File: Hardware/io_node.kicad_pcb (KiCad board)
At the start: 2 copper layers, 60 x 90 mm, 133 parts, among them J1 Conn_01x09, J2 Conn_01x09, J3 Conn_01x09, J4 Conn_01x05, J5 USB_B_Micro, J6 Conn_01x05, J7 Conn_01x05, J8 Conn_01x02, J9 Conn_01x04, Q1 2N7002, Q2 2N7002, Q3 2N7002, Q4 2N7002, Q5 2N7002, Q6 2N7002, Q7 2N7002, Q8 2N7002, U1 STM32F103RBT6, U10 EL357N-G, U11 EL357N-G, U12 EL357N-G, U13 EL357N-G, U14 EL357N-G, U15 USBLC6-2SC6, U2 AMS1117-5.0, U3 AMS1117-3.3, U4 SP3485EN, U5 TLV274CPWR, U6 TLV274CPWR, U7 EL357N-G, U8 EL357N-G, U9 EL357N-G, Y1 8 MHz

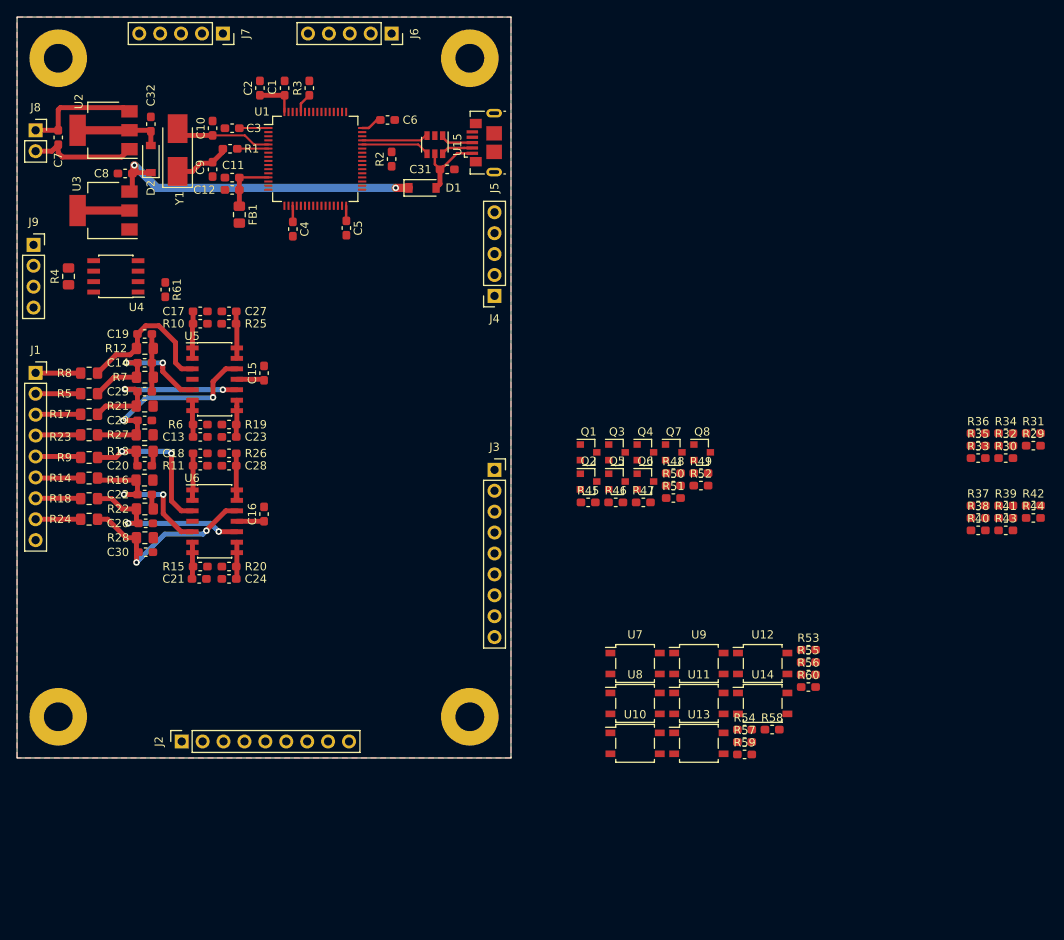
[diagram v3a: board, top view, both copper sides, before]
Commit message: Layout DIN DOT
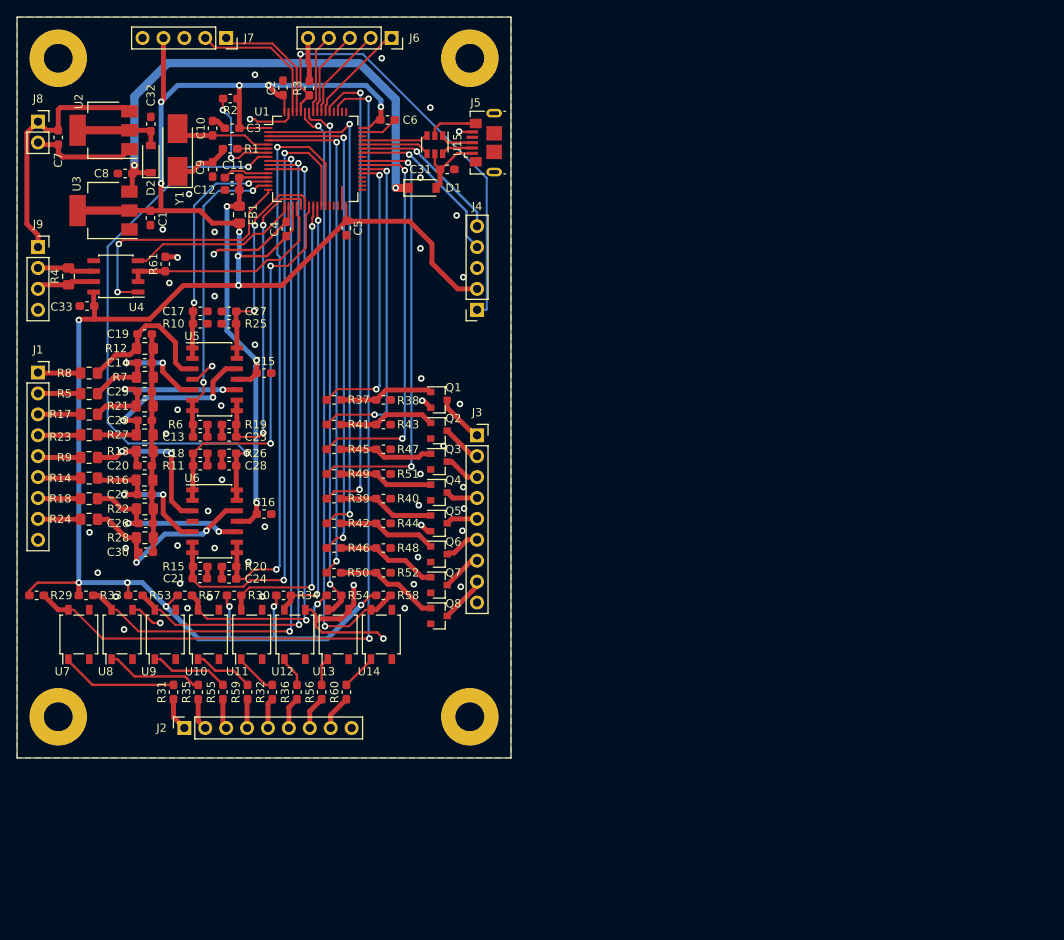
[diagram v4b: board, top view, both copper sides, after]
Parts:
- added C33: 100NF, Capacitor_SMD:C_0603_1608Metric_Pad1.05x0.95mm_HandSolder, F.Cu at (53.5, 50.1)
- moved R29 122.4 mm to (47.4, 85.2)
- moved R33 109.7 mm to (53.4, 85.2)
- moved R31 109.1 mm to (64.0, 97.0), turned to 90 degrees
- moved R35 99.4 mm to (67.0, 97.0), turned to 90 degrees
- moved R30 95.2 mm to (71.4, 85.2)
- moved R32 94.0 mm to (76.0, 97.0), turned to 90 degrees
- moved R34 89.9 mm to (77.4, 85.2)
- moved R36 88.5 mm to (79.0, 97.0), turned to 90 degrees
- moved R42 85.0 mm to (83.5, 76.5)
- moved R41 82.4 mm to (83.5, 64.5)
- moved R53 82.0 mm to (59.4, 85.2)
- moved R39 81.6 mm to (83.5, 73.5)
- moved R37 79.3 mm to (83.5, 61.5)
- moved R44 79.0 mm to (89.5, 76.5)
- moved R43 76.7 mm to (89.5, 64.5)
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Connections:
- Q1 pad 3: /TIM3_CH1 -> /Output/DOT_0
- Q2 pad 3: /OUT_4 -> /Output/DOT_1
- Q3 pad 3: /TIM3_CH2 -> /Output/DOT_2
- Q4 pad 3: /OUT_5 -> /Output/DOT_3
- Q5 pad 3: /TIM3_CH3 -> /Output/DOT_4
- Q6 pad 3: /OUT_6 -> /Output/DOT_5
- Q7 pad 3: /TIM3_CH4 -> /Output/DOT_6
- Q8 pad 3: /OUT_7 -> /Output/DOT_7
- R29 pad 2: /Input/DIN_0 -> /IN_0
- R30 pad 2: /Input/DIN_4 -> /IN_4
- R31 pad 1: /IN_0 -> /Input/DIN_0
- R32 pad 1: /IN_4 -> /Input/DIN_4
- R33 pad 2: /Input/DIN_1 -> /IN_1
- R34 pad 2: /Input/DIN_5 -> /IN_5
- R35 pad 1: /IN_1 -> /Input/DIN_1
- R36 pad 1: /IN_5 -> /Input/DIN_5
- R37 pad 1: /Output/DOT_0 -> /TIM3_CH1
- R39 pad 1: /Output/DOT_4 -> /OUT_4
- R39 pad 2: Net-(Q2-Pad1) -> Net-(Q5-Pad1)
- R40 pad 1: Net-(Q2-Pad1) -> Net-(Q5-Pad1)
- R41 pad 1: /Output/DOT_1 -> /TIM3_CH2
- R41 pad 2: Net-(Q3-Pad1) -> Net-(Q2-Pad1)
- R42 pad 1: /Output/DOT_5 -> /OUT_5
- R42 pad 2: Net-(Q4-Pad1) -> Net-(Q6-Pad1)
- R43 pad 1: Net-(Q3-Pad1) -> Net-(Q2-Pad1)
- R44 pad 1: Net-(Q4-Pad1) -> Net-(Q6-Pad1)
- R45 pad 1: /Output/DOT_2 -> /TIM3_CH3
- R45 pad 2: Net-(Q5-Pad1) -> Net-(Q3-Pad1)
- R46 pad 1: /Output/DOT_6 -> /OUT_6
- R46 pad 2: Net-(Q6-Pad1) -> Net-(Q7-Pad1)
- R47 pad 1: Net-(Q5-Pad1) -> Net-(Q3-Pad1)
- R48 pad 1: Net-(Q6-Pad1) -> Net-(Q7-Pad1)
- R49 pad 1: /Output/DOT_3 -> /TIM3_CH4
- R49 pad 2: Net-(Q7-Pad1) -> Net-(Q4-Pad1)
- R50 pad 1: /Output/DOT_7 -> /OUT_7
- R51 pad 1: Net-(Q7-Pad1) -> Net-(Q4-Pad1)
- R53 pad 2: /Input/DIN_2 -> /IN_2
- R54 pad 2: /Input/DIN_6 -> /IN_6
- R55 pad 1: /IN_2 -> /Input/DIN_2
- R56 pad 1: /IN_6 -> /Input/DIN_6
- R57 pad 2: /Input/DIN_3 -> /IN_3
- R58 pad 2: /Input/DIN_7 -> /IN_7
- R59 pad 1: /IN_3 -> /Input/DIN_3
- R60 pad 1: /IN_7 -> /Input/DIN_7
- U1 pad 28: /SPI1_CS -> Net-(U1-Pad28)
- U1 pad 54: Net-(U1-Pad54) -> /SPI1_CS
- U10 pad 1: Net-(R36-Pad2) -> Net-(R59-Pad2)
- U10 pad 4: /Input/DIN_5 -> /IN_3
- U11 pad 1: Net-(R55-Pad2) -> Net-(R32-Pad2)
- U11 pad 4: /Input/DIN_2 -> /IN_4
- U12 pad 1: Net-(R56-Pad2) -> Net-(R36-Pad2)
- U12 pad 4: /Input/DIN_6 -> /IN_5
- U13 pad 1: Net-(R59-Pad2) -> Net-(R56-Pad2)
- U13 pad 4: /Input/DIN_3 -> /IN_6
- U14 pad 4: /Input/DIN_7 -> /IN_7
- U4 pad 8: +3.3VA -> +3V3
- U7 pad 4: /Input/DIN_0 -> /IN_0
- U8 pad 1: Net-(R32-Pad2) -> Net-(R35-Pad2)
- U8 pad 4: /Input/DIN_4 -> /IN_1
- U9 pad 1: Net-(R35-Pad2) -> Net-(R55-Pad2)
- U9 pad 4: /Input/DIN_1 -> /IN_2
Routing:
- net +3V3: track 21.3 -> 271.9 mm, vias 0 -> 16
- net /IN_0: track 0.00 -> 112.2 mm, vias 0 -> 2
- net GND: track 24.0 -> 125.2 mm, vias 0 -> 53
- net /IN_1: track 0.00 -> 86.1 mm, vias 0 -> 2
- net /IN_2: track 0.00 -> 80.5 mm, vias 0 -> 2
- net /IN_3: track 0.00 -> 75.0 mm, vias 0 -> 2
- net /ADC_IN8: track 4.48 -> 78.3 mm, vias 0 -> 2
- net /IN_7: track 0.00 -> 73.4 mm, vias 0 -> 2
- net /ADC_IN9: track 4.49 -> 73.2 mm, vias 0 -> 2
- net /ADC_IN10: track 6.49 -> 71.6 mm, vias 0 -> 2
- net /IN_6: track 0.00 -> 64.0 mm, vias 0 -> 2
- net /OUT_7: track 0.00 -> 61.2 mm, vias 0 -> 2
- net /OUT_5: track 0.00 -> 60.9 mm, vias 0 -> 2
- net /OUT_6: track 0.00 -> 60.4 mm, vias 0 -> 2
- net /OUT_4: track 0.00 -> 57.8 mm, vias 0 -> 2
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
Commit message: Add SWD
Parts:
- added J10: Conn_01x04, Connector_PinSocket_2.54mm:PinSocket_1x04_P2.54mm_Vertical, F.Cu at (93.3, 17.5)
- moved J6 7.40 mm to (83.1, 17.5)
- moved J7 2.54 mm to (67.9, 17.5)
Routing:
- net /NRST: track 12.4 -> 45.7 mm, vias 2 -> 3
- net /ADC_IN10: track 71.6 -> 53.3 mm
- net /SWDIO: track 0.00 -> 14.1 mm
- net /SWCLK: track 0.00 -> 13.9 mm
- net GND: track 125.2 -> 134.0 mm, vias 53 -> 135
- net /SPI1_MOSI: track 9.77 -> 13.1 mm
- net /SPI1_CS: track 12.6 -> 9.24 mm
- net /USART2_TX: track 31.1 -> 28.1 mm
- net /BOOT0: track 53.9 -> 51.6 mm
- net /I2C1_SCL: track 15.4 -> 17.3 mm
- net /I2C1_SDA: track 17.4 -> 19.2 mm
- net /SPI1_SCK: track 11.5 -> 9.76 mm
- net +5V: track 61.7 -> 60.4 mm
- net +3V3: track 271.9 -> 272.7 mm
- net /ADC_IN9: track 73.2 -> 72.5 mm
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
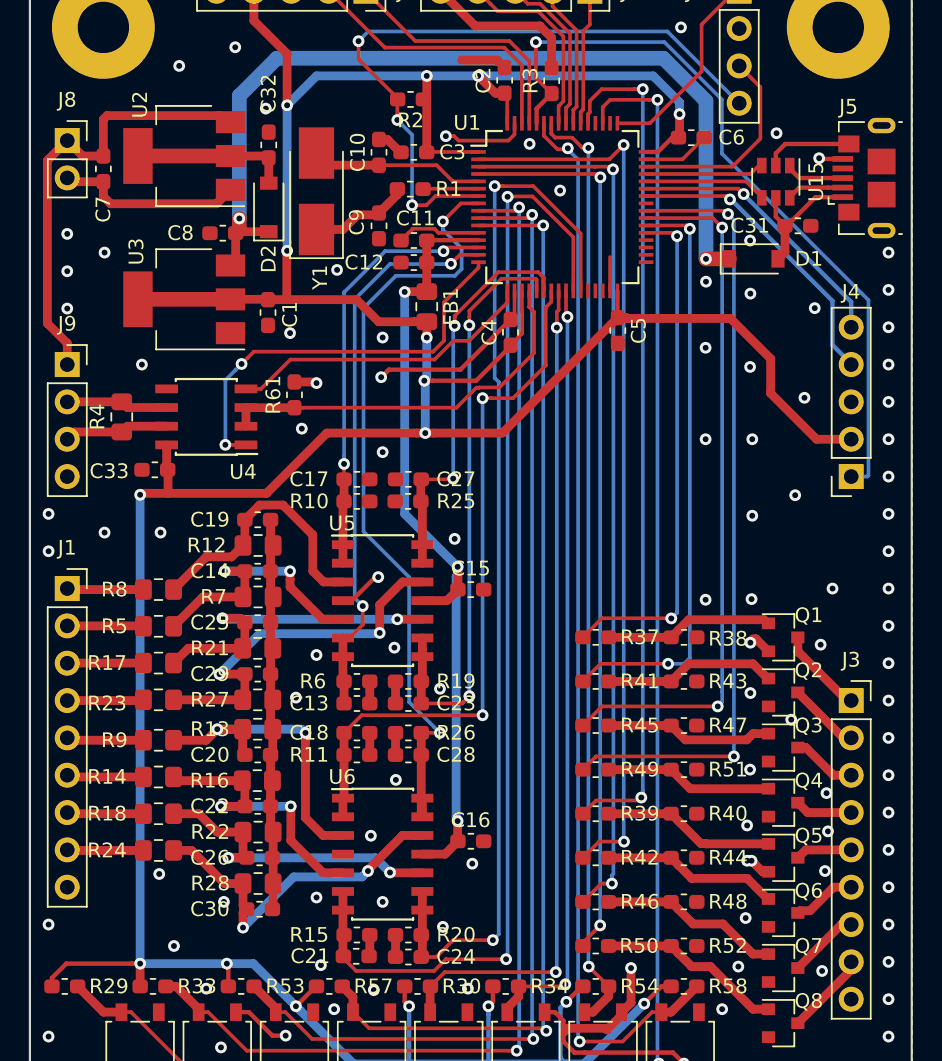
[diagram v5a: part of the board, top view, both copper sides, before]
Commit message: Update USB footprint
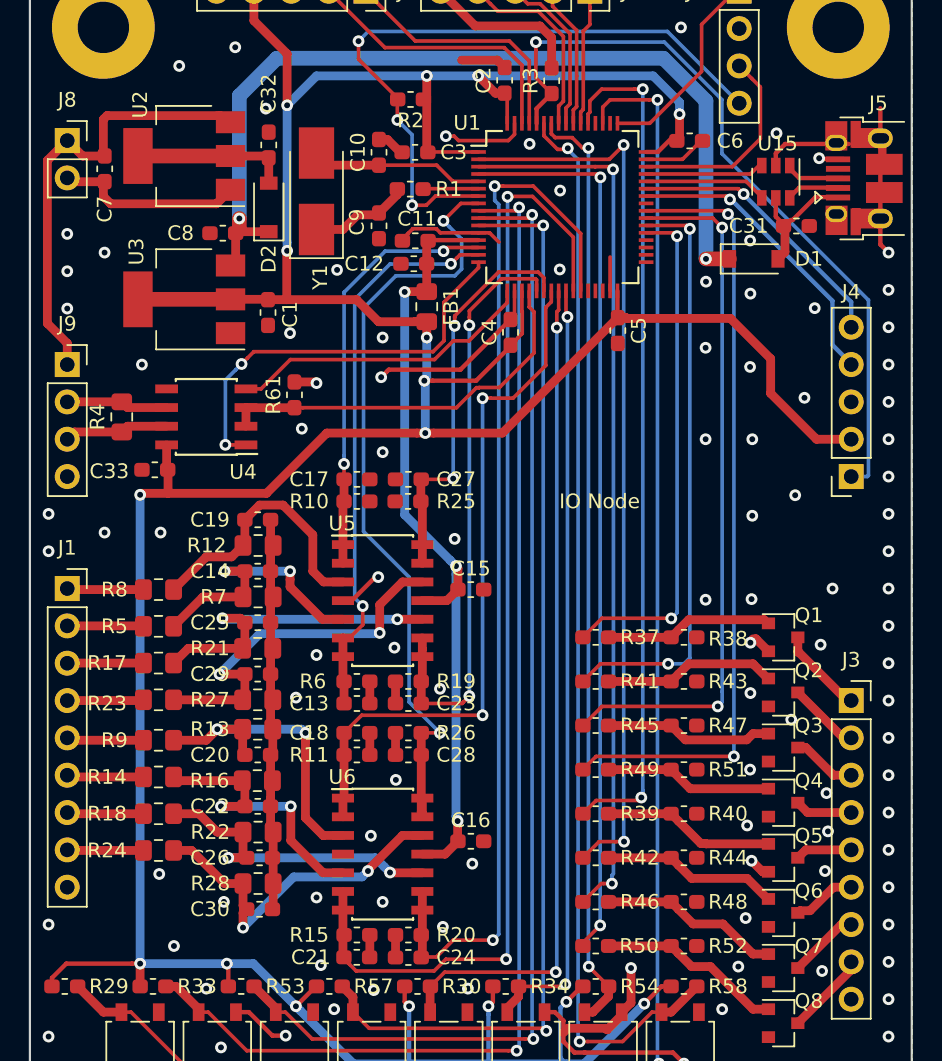
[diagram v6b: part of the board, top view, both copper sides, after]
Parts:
- J5: footprint Connector_USB:USB_Micro-B_GCT_USB3076-30-A -> Connector_USB:USB_Micro-B_Amphenol_10103594-0001LF_Horizontal
- moved C6 0.25 mm to (89.9, 27.7)
- moved C31 0.10 mm to (97.2, 33.5)
- moved C11 0.10 mm to (71.2, 34.5)
- moved C7 0.09 mm to (50.1, 29.6)
- moved C21 0.08 mm to (67.2, 83.3)
- moved C12 0.08 mm to (71.1, 36.1)
- moved C3 0.08 mm to (71.2, 28.5)
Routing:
- net GND: track 134.0 -> 147.6 mm
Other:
- board text added: "IO Node"
